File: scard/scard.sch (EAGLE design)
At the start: 66 parts, among them Q1 FDN360P, X1 COAX, X2 1365-20

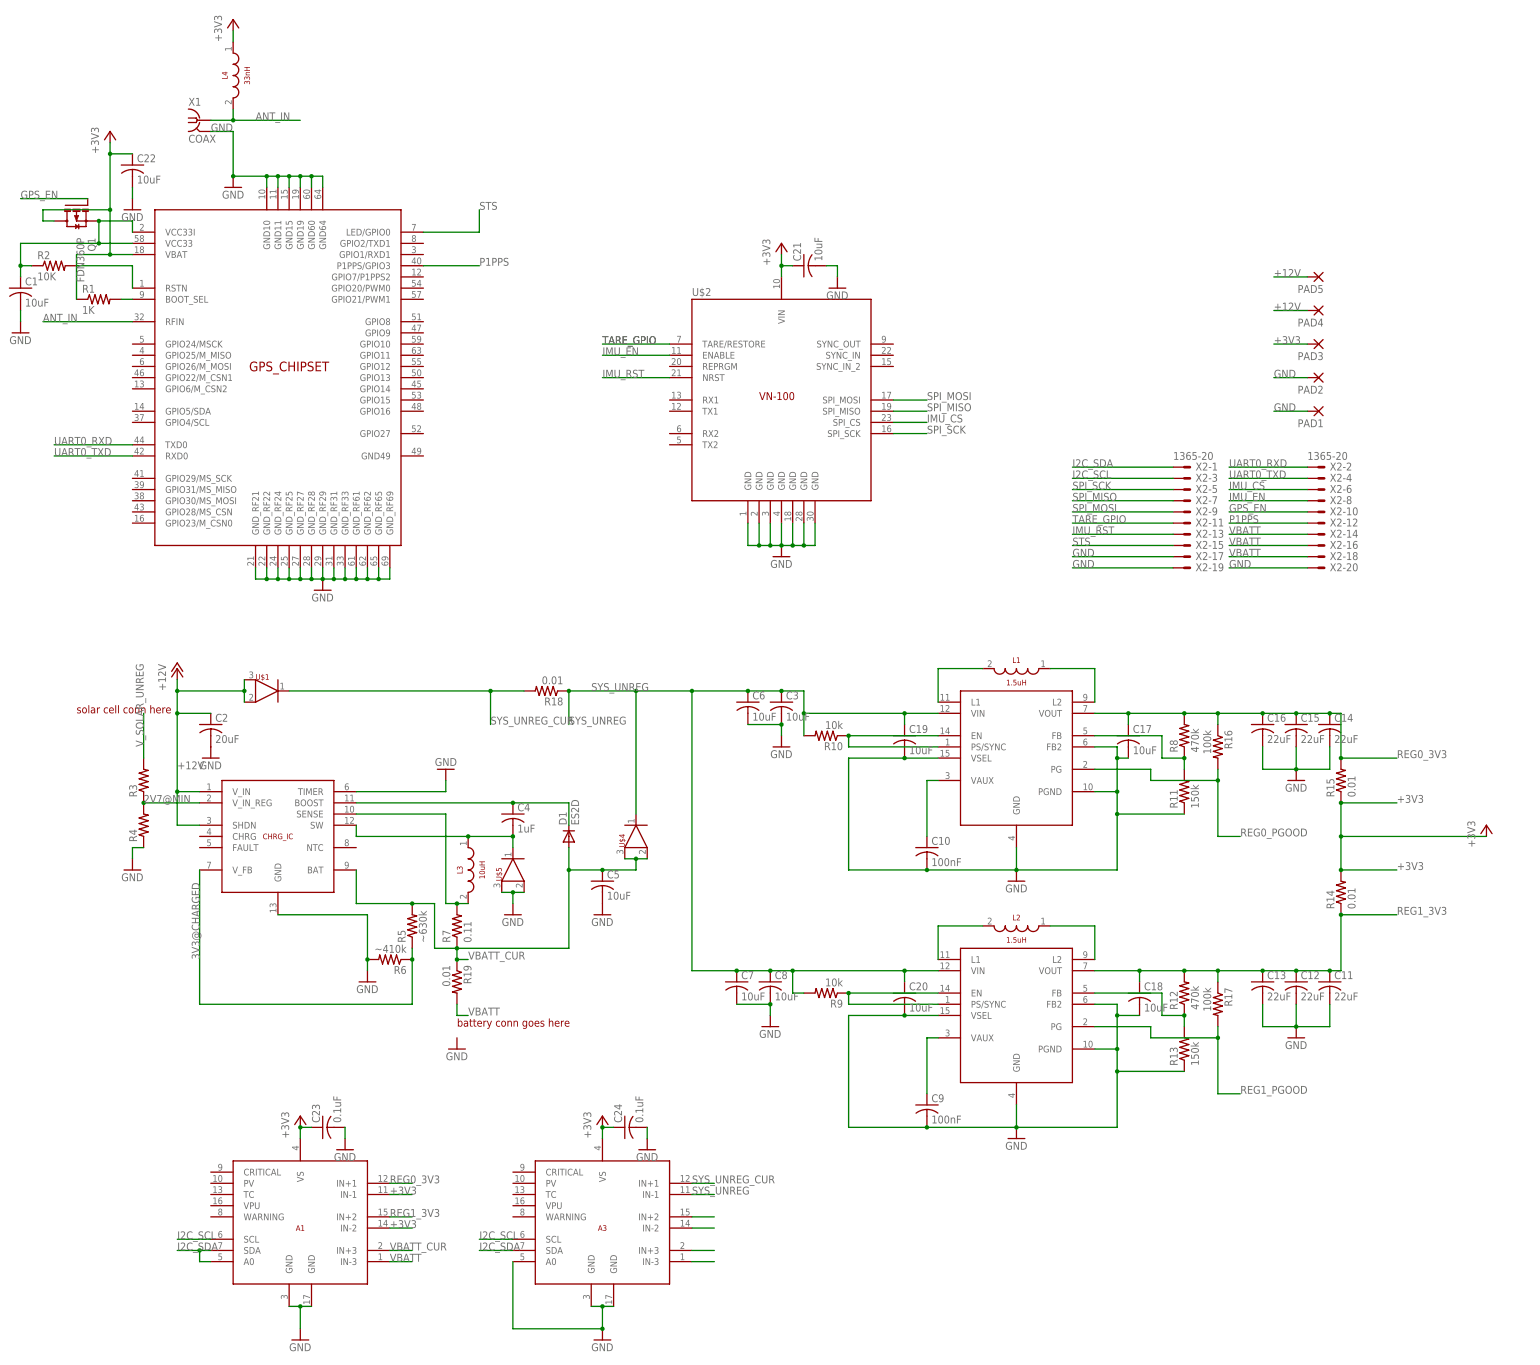
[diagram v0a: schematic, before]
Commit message: need switching voltage regulator capable of up to 8A
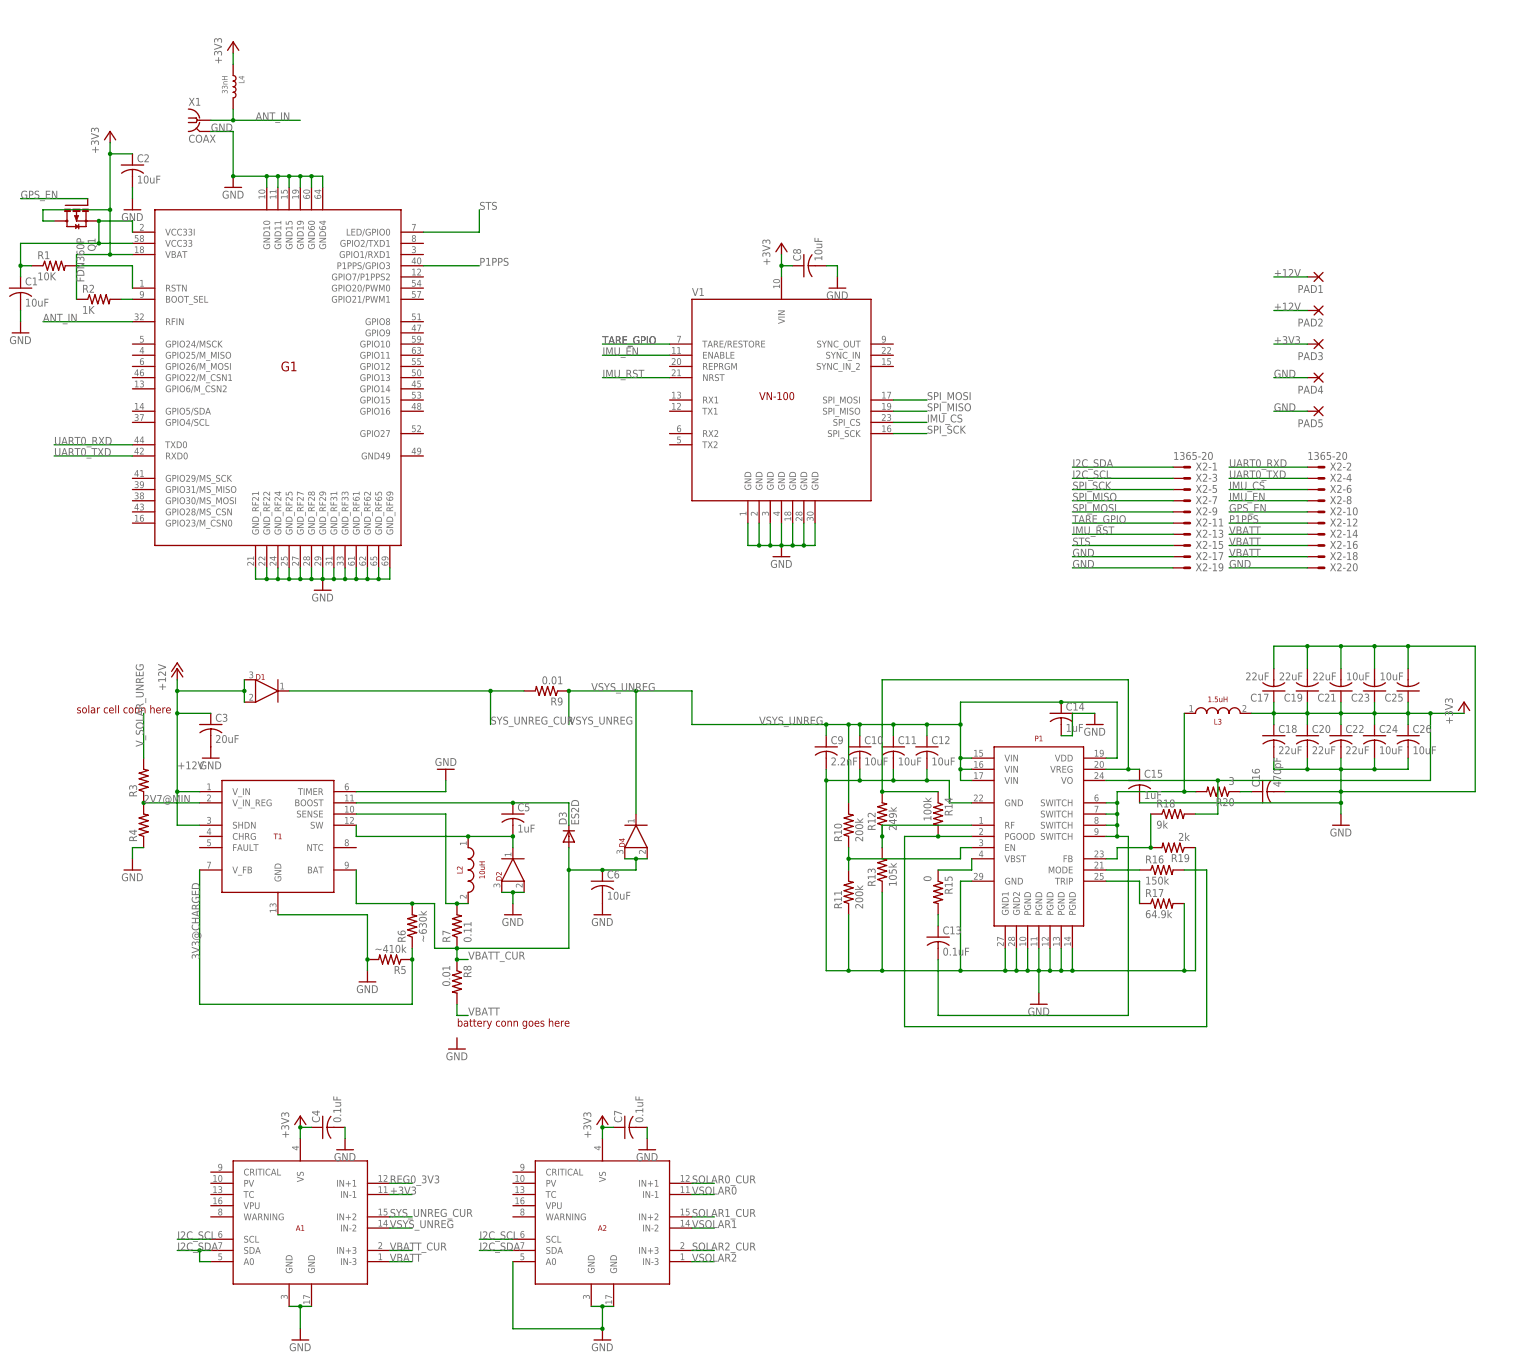
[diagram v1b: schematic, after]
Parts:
- removed L1: 1.5uH, calsat:XFL4020
- removed U$1: B085BM30, calsat:B085BM30
- removed U$6, U$7: TPS63070, calsat:TPS63070
- added C25, C26: 10uF, resistor:C-USC0603
- added D3: ES2D, diode:ES2D
- added P1: TPS548A20, calsat:TPS548A20
- added R20: 3, rcl:R-US_R0402
- C10: value 100nF -> 10uF; device rcl:C-USC0603 -> resistor:C-USC0603
- C11, C12: value 22uF -> 10uF; device rcl:C-USC0805 -> resistor:C-USC0603
- C13: value 22uF -> 0.1uF; device rcl:C-USC0805 -> resistor:C-USC0402
- C14, C15: value 22uF -> 1uF; device rcl:C-USC0805 -> resistor:C-USC0402
- C16: value 22uF -> 470pF; device rcl:C-USC0805 -> resistor:C-USC0402
- C17, C18, C19, C20: value 10uF -> 22uF; device rcl:C-USC0603 -> resistor:C-USC0603
- C2: value 20uF -> 10uF; device resistor:C-USC0805 -> resistor:C-USC0603
- C21, C22: value 10uF -> 22uF
- C23, C24: value 0.1uF -> 10uF
- C3: value 10uF -> 20uF; device rcl:C-USC0805 -> resistor:C-USC0805
- C4: value 1uF -> 0.1uF; device resistor:C-USC0805 -> resistor:C-USC0603
- C5: value 10uF -> 1uF
- C6: device rcl:C-USC0805 -> resistor:C-USC0805
- C7: value 10uF -> 0.1uF; device rcl:C-USC0805 -> resistor:C-USC0603
- C8: device rcl:C-USC0805 -> resistor:C-USC0603
- C9: value 100nF -> 2.2nF; device rcl:C-USC0603 -> resistor:C-USC0402
- D1: value ES2D -> B085BM30; device diode:ES2D -> calsat:B085BM30
- L2: value 1.5uH -> 10uH; device calsat:XFL4020 -> calsat:SRP7028A
- L3: value 10uH -> 1.5uH; device calsat:XFL4020 -> calsat:SRP7028A
- L4: device calsat:XFL4020 -> Seeed-Inductor:SMD-FERRITE-BEAD-330R-1500MA(0805)'0805'
- R1: value 1K -> 10K
- R10: value 10k -> 200k; device resistor:R-US_R0603 -> rcl:R-US_R0402
- R11: value 150k -> 200k; device resistor:R-US_R0603 -> rcl:R-US_R0402
- R12: value 470k -> 249k; device resistor:R-US_R0603 -> rcl:R-US_R0402
- R13: value 150k -> 105k; device resistor:R-US_R0603 -> rcl:R-US_R0402
- R14: value 0.01 -> 100k; device resistor:R-US_R1210 -> rcl:R-US_R0402
- R15: value 0.01 -> 0; device resistor:R-US_R1210 -> rcl:R-US_R0402
- R16: value 100k -> 150k; device resistor:R-US_R0603 -> rcl:R-US_R0402
- R17: value 100k -> 64.9k; device resistor:R-US_R0603 -> rcl:R-US_R0402
- R18: value 0.01 -> 9k; device resistor:R-US_R1210 -> rcl:R-US_R0402
- R19: value 0.01 -> 2k; device resistor:R-US_R1210 -> rcl:R-US_R0402
- R2: value 10K -> 1K
- R5: value ~630k -> ~410k
- R6: value ~410k -> ~630k
- R8: value 470k -> 0.01; device resistor:R-US_R0603 -> resistor:R-US_R1210
- R9: value 10k -> 0.01; device resistor:R-US_R0603 -> resistor:R-US_R1210
- renumbered A3 to A2, CHRG_IC to T1, GPS_CHIPSET to G1, U$2 to V1, U$4 to D4, U$5 to D2
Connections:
- net N$32 renamed SOLAR1_CUR
- net N$33 renamed VSOLAR1
- net N$34 renamed SOLAR2_CUR
- net N$35 renamed VSOLAR2
- removed net REG0_EN: R10.1, U$6.EN, U$6.PS/SYNC
- removed net REG0_PGOOD: R16.2, U$6.PG
- removed net REG1_3V3: A1.IN+2, C11.1, C12.1, C13.1, C18.1, R12.2, R14.1, R17.1, U$7.VOUT
- removed net REG1_EN: R9.1, U$7.EN, U$7.PS/SYNC
- removed net REG1_PGOOD: R17.2, U$7.PG
- removed net SYS_UNREG: A2.IN-1, C19.1, C20.1, C3.1, C6.1, C7.1, C8.1, D4.@3, R10.2, R18.1, R9.2, U$6.VIN, U$7.VIN
- new net N$1: P1.MODE, R16.1
- new net N$17: C16.1, R20.1
- new net N$2: C13.2, L3.@1, P1.SWITCH@1, P1.SWITCH@2, P1.SWITCH@3, P1.SWITCH@4, R20.2
- new net SOLAR0_CUR: A2.IN+1
- new net VSOLAR0: A2.IN-1
- new net VSYS_UNREG: A1.IN-2, C10.1, C11.1, C12.1, C14.1, C9.1, D4.@3, P1.VDD, P1.VIN@1, P1.VIN@2, P1.VIN@3, R10.2, R9.1
- net +12V: now also C3.1, D1.@1, D1.@2, PAD1.P, PAD2.P; no longer C2.1, PAD4.P, PAD5.P, U$1.@1, U$1.@2
- net +3V3: now also C17.1, C18.1, C19.1, C2.1, C20.1, C25.1, C26.1, C4.1, C7.1, C8.1, L3.@2, L4.1, P1.VO, R18.2, R2.1; no longer A1.IN-2, L4.@1, R1.1, R14.2, R15.1
- net ANT_IN: now also L4.2; no longer L4.@2
- net GND: now also C25.2, C26.2, C4.2, P1.GND, P1.GND1, P1.GND2, P1.GND@3, P1.PGND@1, P1.PGND@2, P1.PGND@3, P1.PGND@4, P1.PGND@5, PAD4.P, PAD5.P, R17.2, R19.1, R5.2; no longer C13.2, C5.2, PAD1.P, PAD2.P, R6.2, U$6.FB2, U$6.GND, U$6.PGND, U$6.VSEL, U$7.FB2, U$7.GND, U$7.PGND, U$7.VSEL
- net N$10: now also C15.1, P1.VREG, R12.2, R14.1; no longer R12.1, R13.2, U$7.FB
- net N$11: now also P1.RF, R12.1, R13.2; no longer L2.@2, U$7.L1
- net N$12: now also P1.PGOOD, R14.2, R16.2; no longer L2.@1, U$7.L2
- net N$13: now also P1.TRIP, R17.1; no longer L1.@1, U$6.L2
- net N$14: now also P1.FB, R18.1, R19.2; no longer R11.2, R8.1, U$6.FB
- net N$15: now also P1.EN, R10.1, R11.2; no longer L1.@2, U$6.L1
- net N$22: now also R1.1; no longer R2.1
- net N$3: now also C5.1, D3.C; no longer C4.1, D1.C
- net N$4: now also C5.2, L2.@1; no longer C4.2, L3.@1
- net N$5: now also P1.VBST, R15.1; no longer C9.1, U$7.VAUX
- net N$6: now also L2.@2; no longer L3.@2
- net N$7: now also R2.2; no longer R1.2
- net N$8: now also R1.2; no longer R2.2
- net N$9: now also C13.1, R15.2; no longer C10.1, U$6.VAUX
- net REG0_3V3: no longer C14.1, C15.1, C16.1, C17.1, R15.2, R16.1, R8.2, U$6.VOUT
- net SYS_UNREG_CUR: now also A1.IN+2, D1.@3, R9.2; no longer A2.IN+1, R18.2, U$1.@3
- net VBATT: now also R8.2; no longer R19.2
- net VBATT_CUR: now also C6.1, D3.A, R6.2, R8.1; no longer C5.1, D1.A, R19.1, R5.2
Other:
- moved on the sheet: C10, C11, C12, C13, C14, C15, C16, C17, C18, C19, C2, C20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

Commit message: Andrea's changes, including routing power supply components, gps thermal vias, and more capacitors
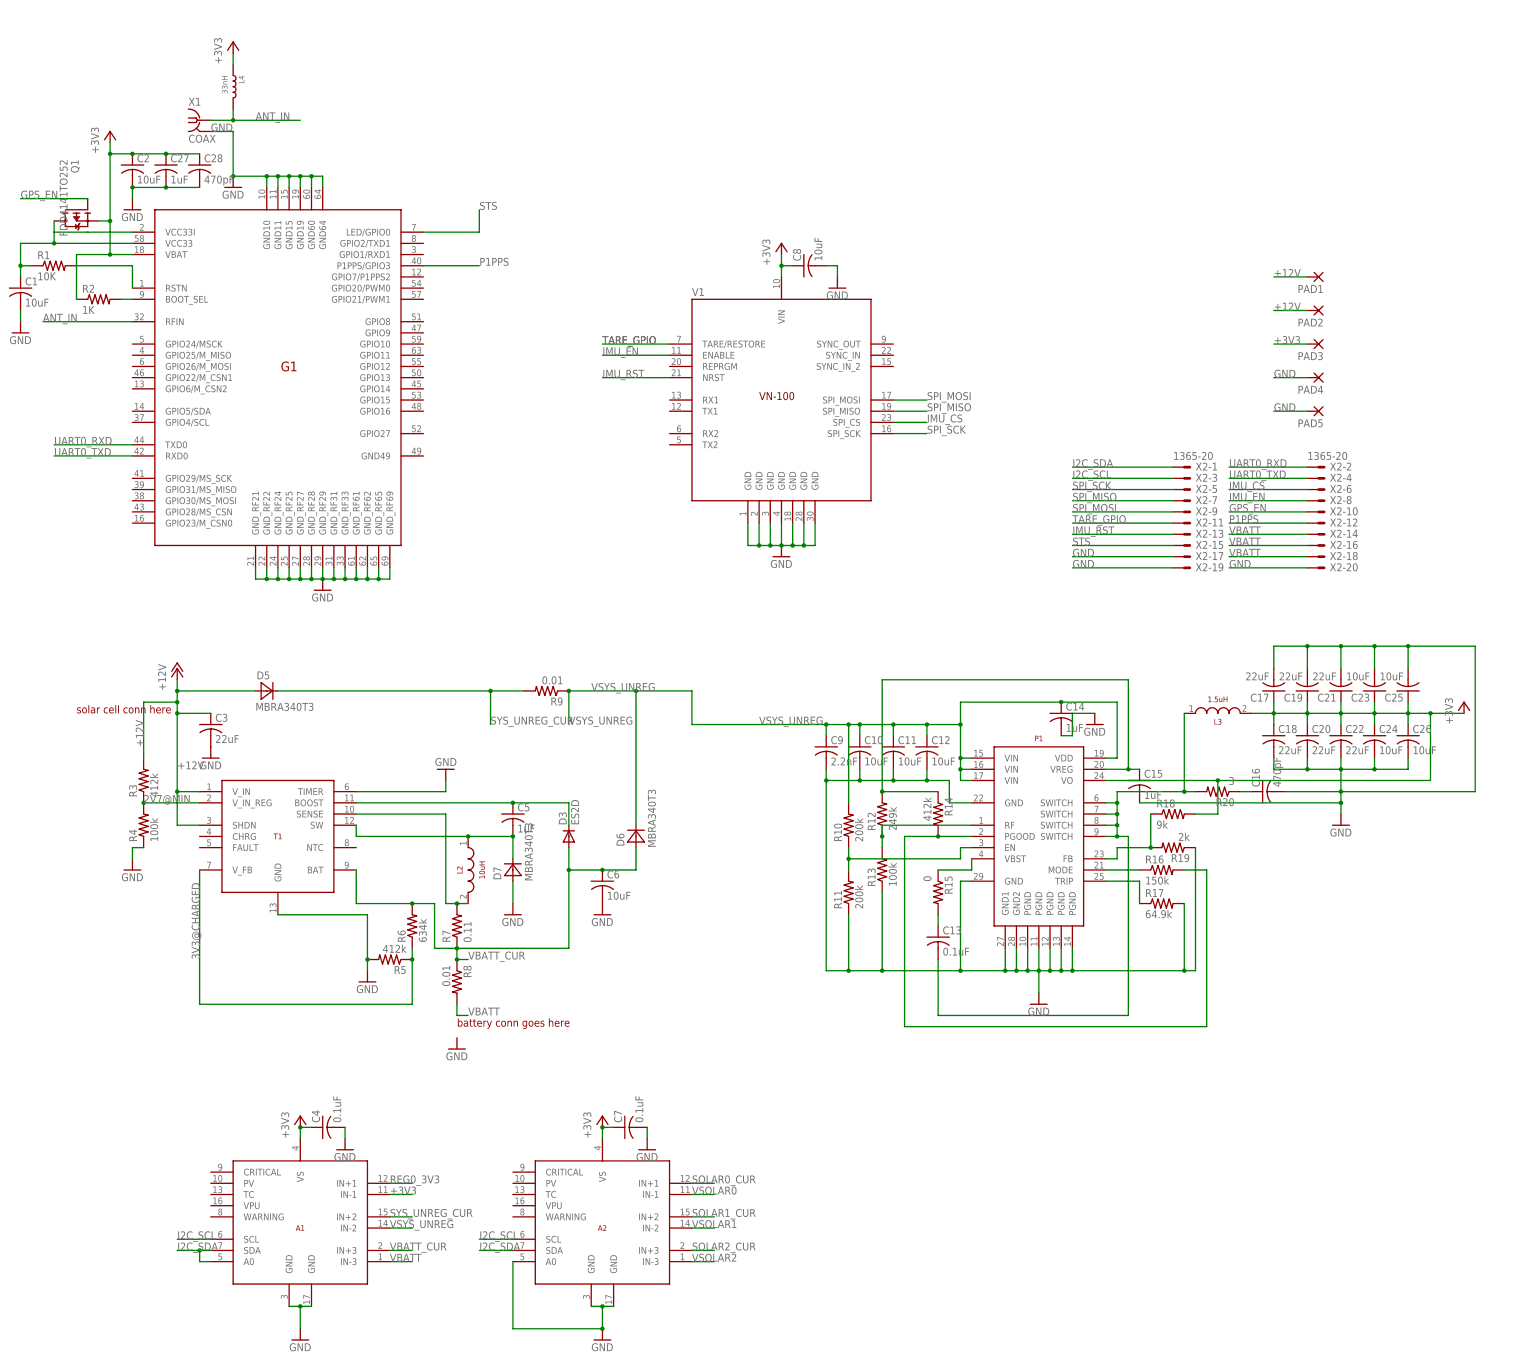
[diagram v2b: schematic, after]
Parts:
- removed D1, D2, D4: B085BM30, calsat:B085BM30
- added C27: 1uF, resistor:C-USC0402
- added C28: 470pF, resistor:C-USC0402
- added D5, D6, D7: MBRA340T3, diode:MBRA340T3
- C17, C18, C19, C20, C21, C22: device resistor:C-USC0603 -> rcl:C-USC0805
- C3: value 20uF -> 22uF
- C5: device resistor:C-USC0805 -> rcl:C-USC0402
- Q1: value FDN360P -> FDD4141TO252; device transistor-power:FDN360P -> transistor-fet:FDD4141TO252
- R1: device resistor:R-US_R0603 -> rcl:R-US_R0603
- R10, R11, R12, R15, R16, R17, R18, R19, R20: device rcl:R-US_R0402 -> rcl:R-US_R0603
- R13: value 105k -> 100k; device rcl:R-US_R0402 -> rcl:R-US_R0603
- R14: value 100k -> 412k; device rcl:R-US_R0402 -> rcl:R-US_R0603
- R3: value (none) -> 412k; device resistor:R-US_R0402 -> rcl:R-US_R0603
- R4: value (none) -> 100k; device resistor:R-US_R0402 -> rcl:R-US_R0603
- R5: value ~410k -> 412k; device resistor:R-US_R0402 -> rcl:R-US_R0603
- R6: value ~630k -> 634k; device resistor:R-US_R0402 -> rcl:R-US_R0603
- R7: device resistor:R-US_R0402 -> rcl:R-US_R0603
- R8, R9: device resistor:R-US_R1210 -> rcl:R-US_R0603
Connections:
- removed net N$22: C1.1, G1.VCC33, G1.VCC33I, Q1.S, R1.1
- removed net V_SOLAR_UNREG: R3.2
- new net N$16: C1.1, G1.VCC33, G1.VCC33I, Q1.D, R1.1
- net +12V: now also D5.A, R3.2; no longer D1.@1, D1.@2
- net +3V3: now also C27.1, C28.1, Q1.S; no longer Q1.D
- net GND: now also C27.2, C28.2, D7.A; no longer D2.@1, D2.@2
- net N$4: now also D7.C; no longer D2.@3
- net SYS_UNREG_CUR: now also D5.C; no longer D1.@3
- net VBATT_CUR: now also D6.A; no longer D4.@1, D4.@2
- net VSYS_UNREG: now also D6.C; no longer D4.@3

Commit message: final DRC fixes
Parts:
- added R21: 0.01, rcl:R-US_R0603
- Q1: value FDD4141TO252 -> FDN360P; device transistor-fet:FDD4141TO252 -> transistor-power:FDN360P
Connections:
- net +3V3: now also R21.1; no longer L3.@2
- net REG0_3V3: now also L3.@2, R21.2
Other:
- moved on the sheet: C17, C18, C19, C20, C21, C22, C23, C24, C25, C26
